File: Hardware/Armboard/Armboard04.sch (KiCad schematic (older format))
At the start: 18 parts

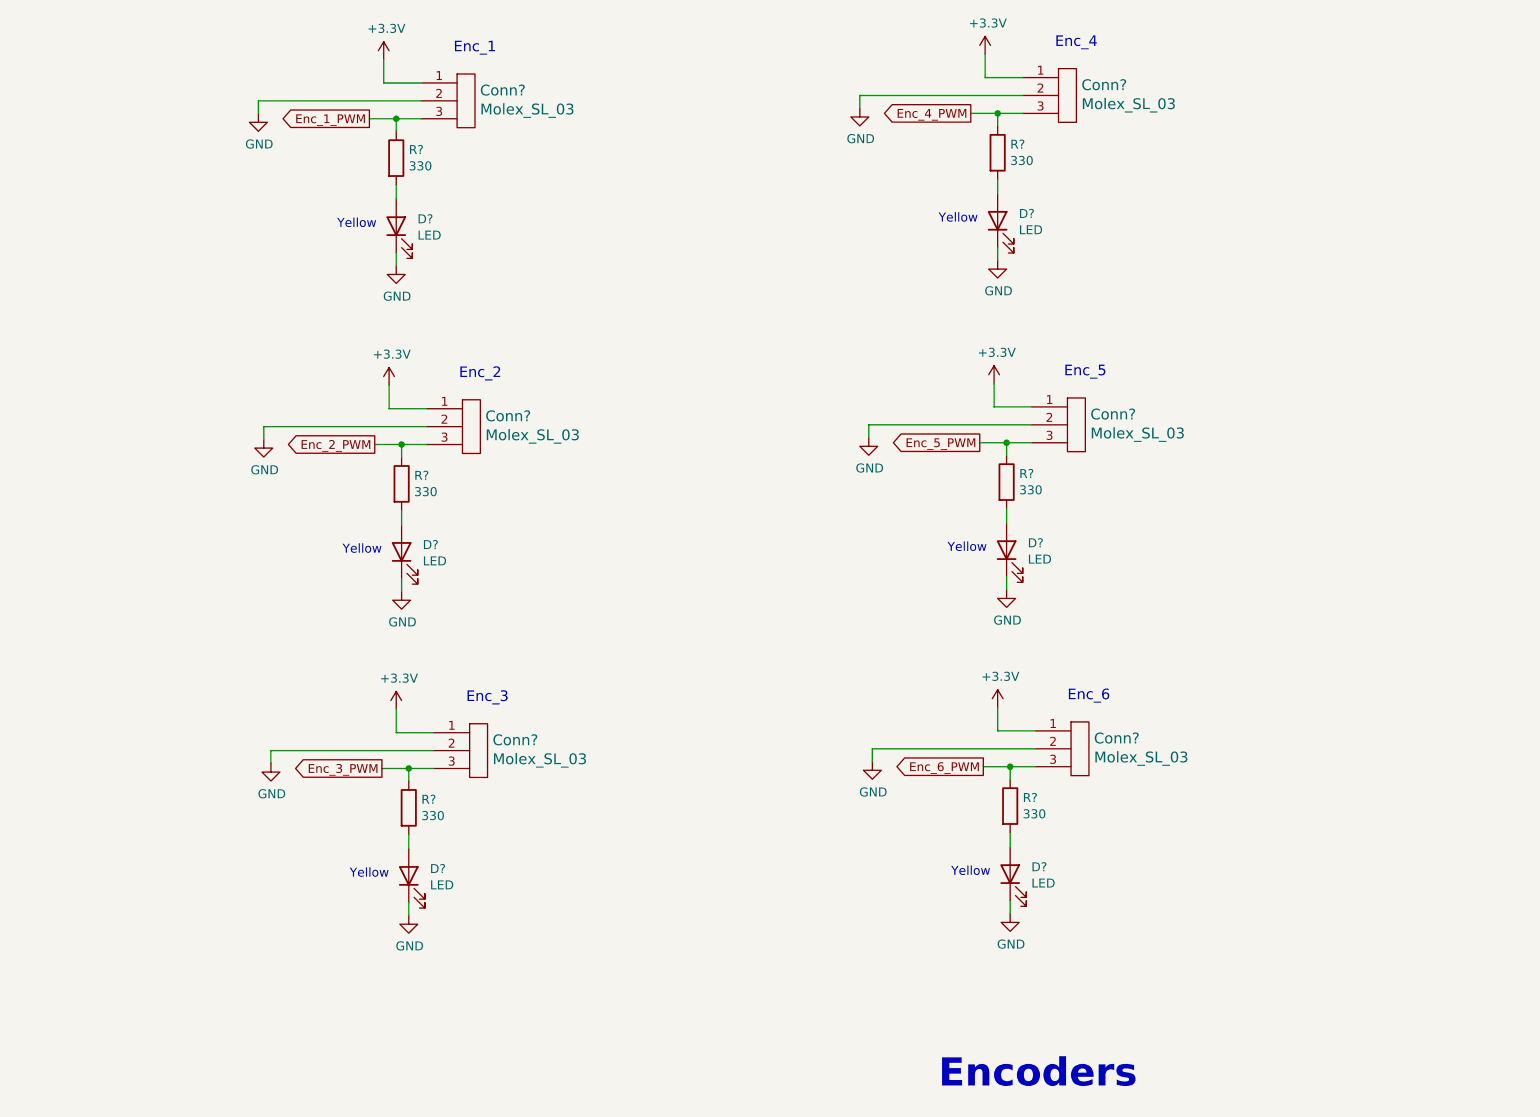
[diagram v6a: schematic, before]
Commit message: Added Software LEDs
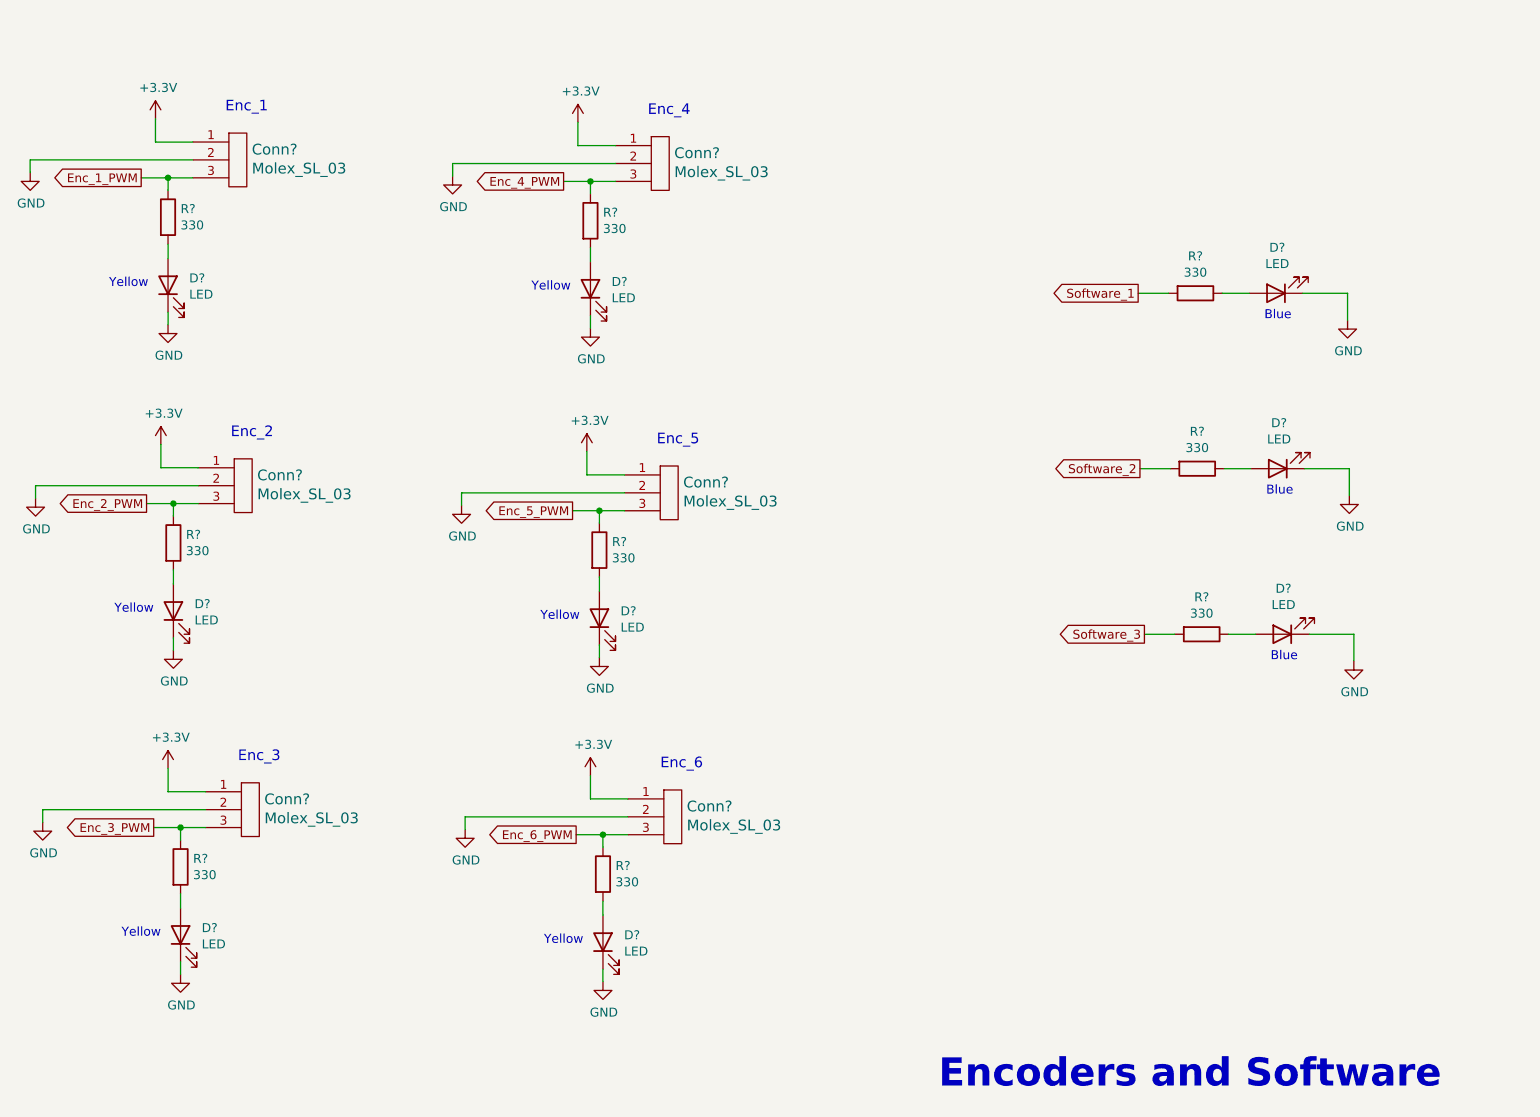
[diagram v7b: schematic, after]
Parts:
- added D? (x3): LED, symbol Device:LED
- added R? (x3): 330, symbol Device:R
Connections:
- net GND: now also D?.1 (K), D?.1 (K), D?.1 (K)
- new net: D?.2 (A), R?.1 (x3)
- new net Software_1: R?.2
- new net Software_2: R?.2
- new net Software_3: R?.2
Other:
- note added: "Blue"
- note added: "Encoders and Software"
- note removed: "Encoders"
- moved on the sheet: Conn?, D?, R?
